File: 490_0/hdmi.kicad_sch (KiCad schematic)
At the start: 8 parts, among them J24 467650301, U10 EMI8142MUTAG, U11 EMI8142MUTAG

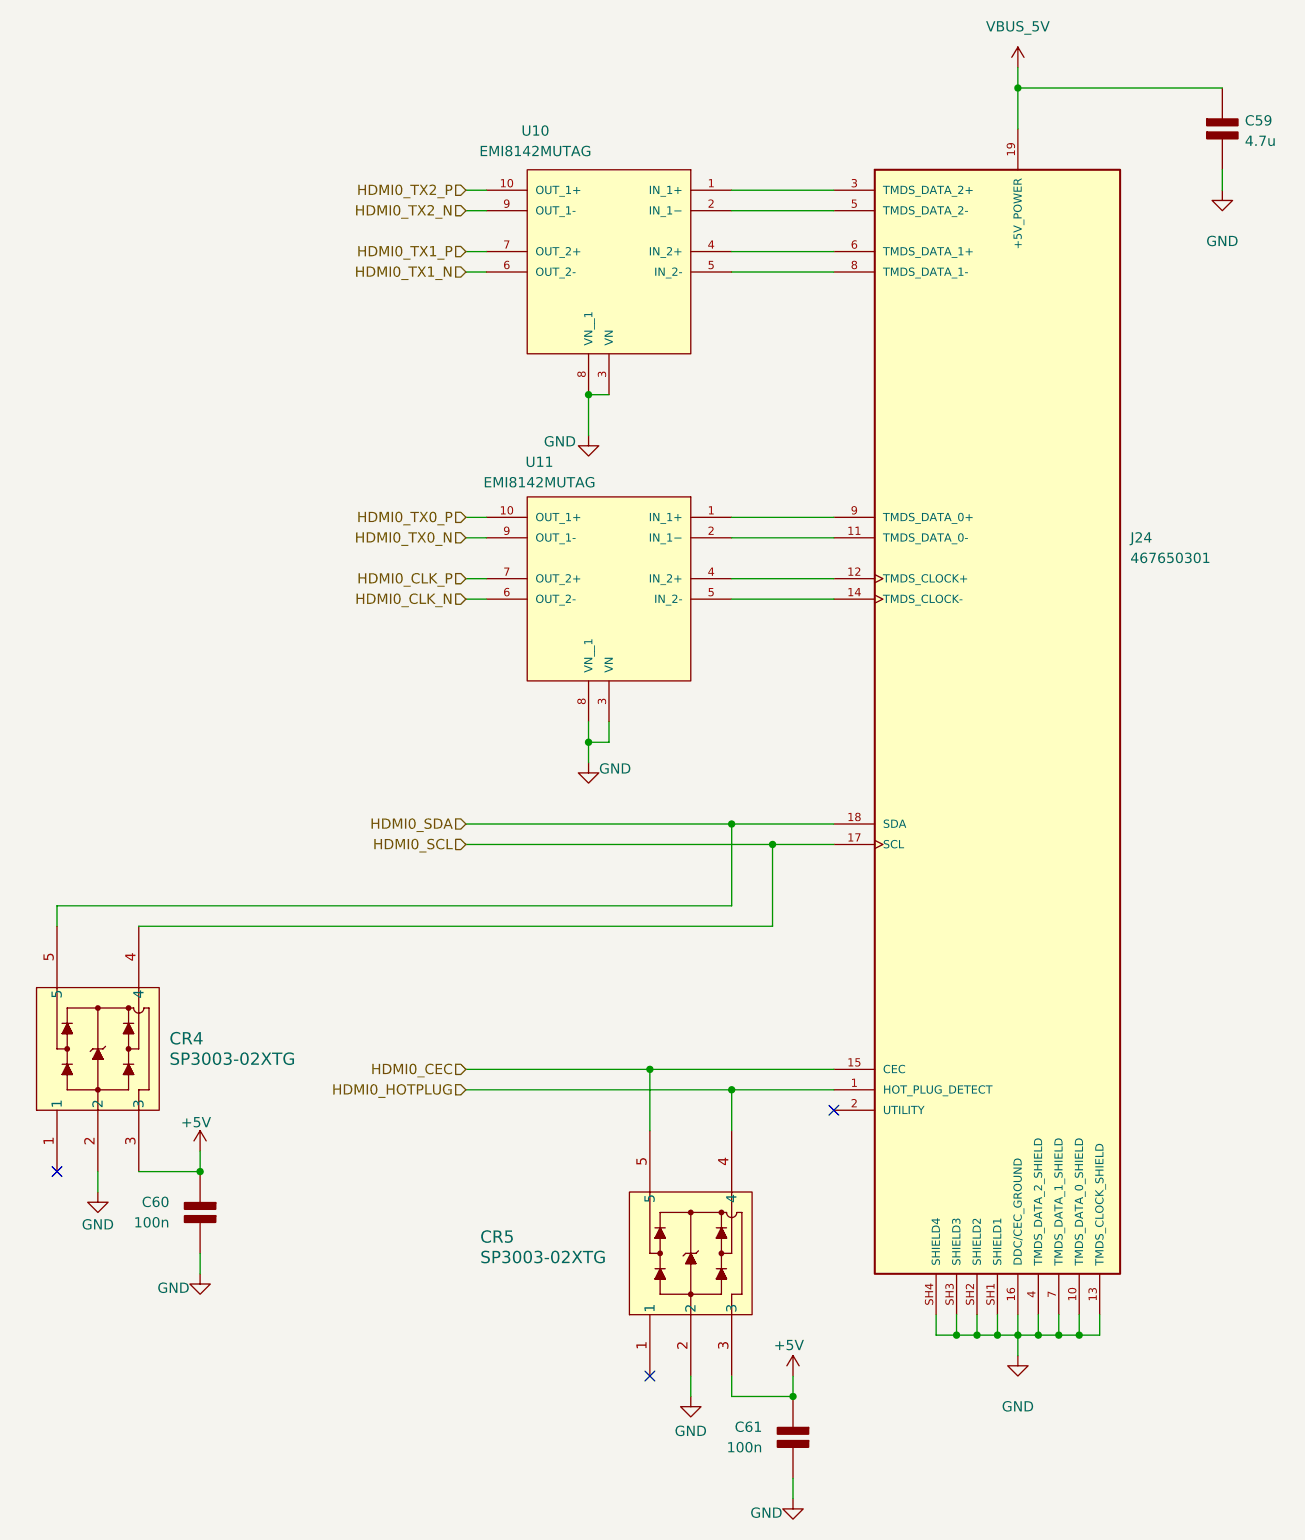
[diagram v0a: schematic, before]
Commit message: Implemented Dmitry comments
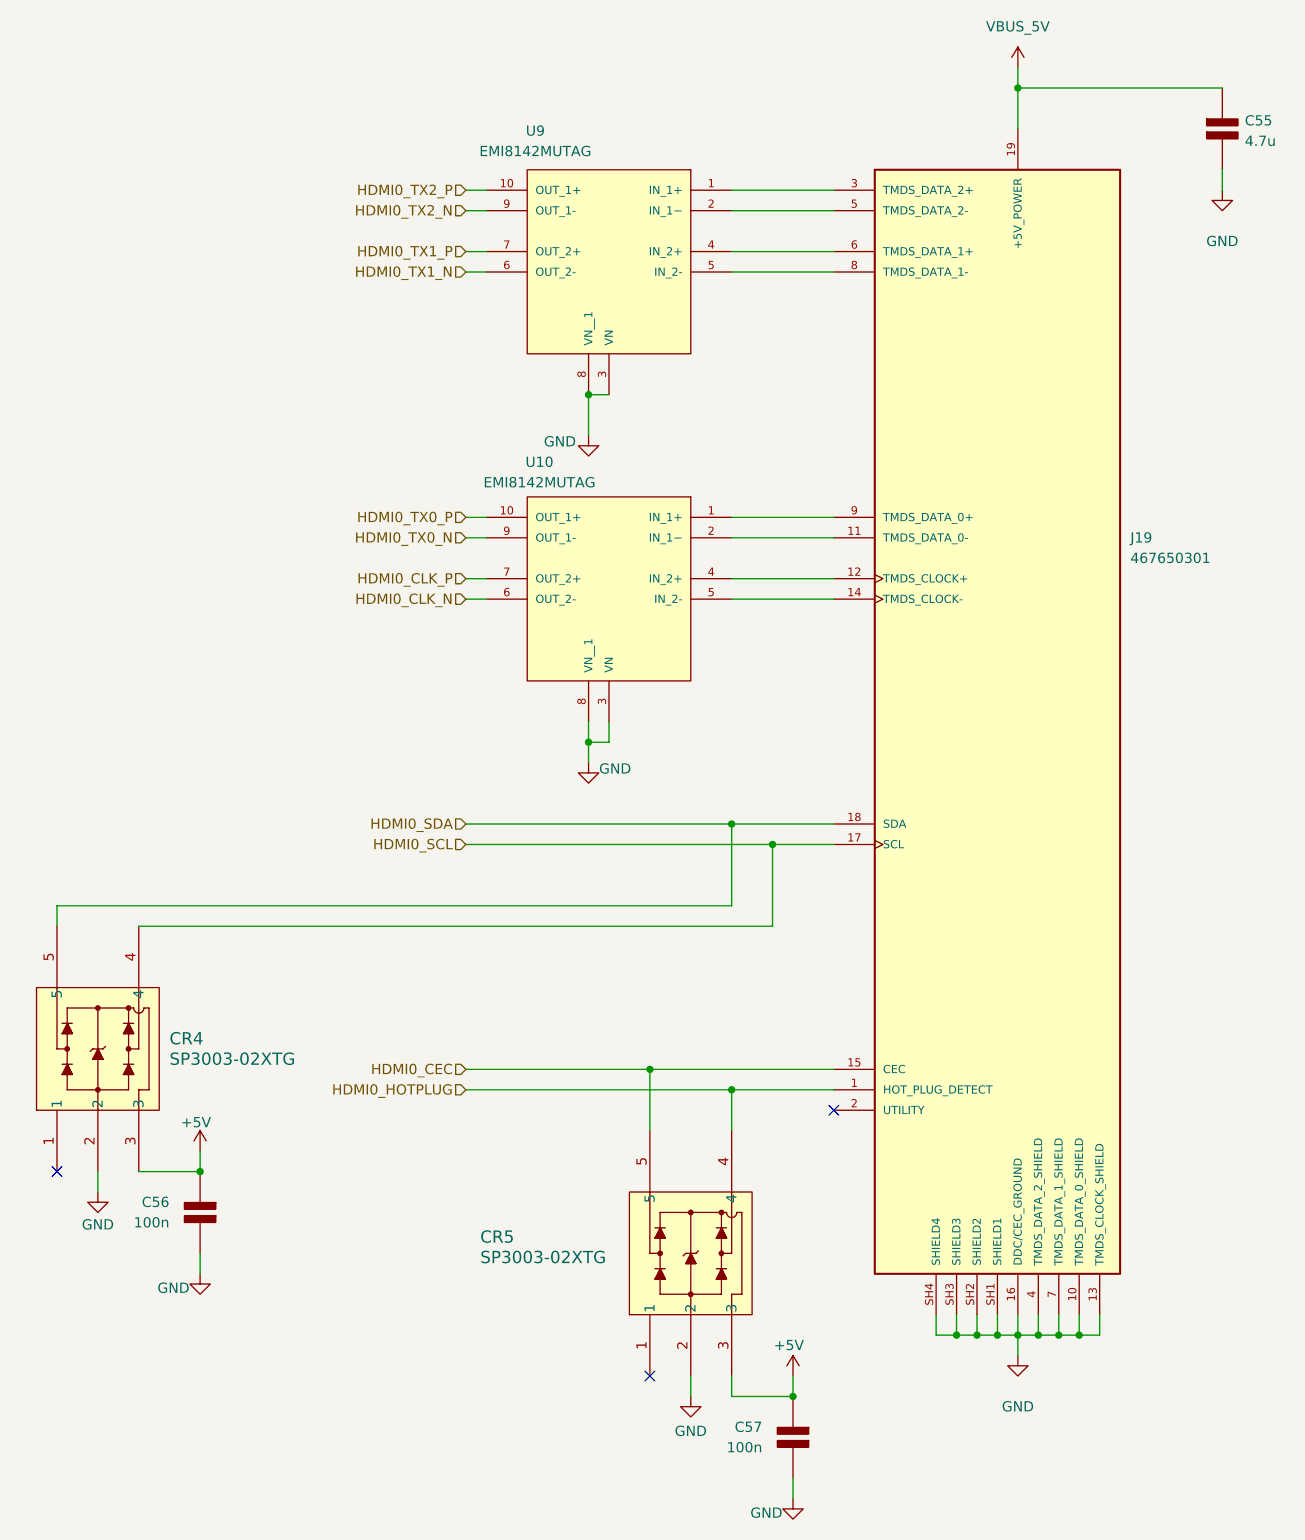
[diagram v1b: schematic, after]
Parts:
- renumbered C59 to C55, C60 to C56, C61 to C57, J24 to J19, U11 to U10, U10 to U9
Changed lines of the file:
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@@
 		(on_board yes)
 		(dnp no)
-		(property "Reference" "#PWR0154"
+		(property "Reference" "#PWR0129"
 			(at 25.4 166.37 0)
 			(effects
@@
 			(project "490_0"
 				(path "/365a82ed-827d-43e1-aa2f-b98221c4179c/f9f22bb2-829e-4ff5-89be-c4b5e2122135/a65b36cc-1b6d-4844-884d-70a990694635"
-					(reference "#PWR0154")
+					(reference "#PWR0129")
 					(unit 1)
 				)
@@
 		(dnp no)
 		(fields_autoplaced yes)
-		(property "Reference" "#PWR0149"
+		(property "Reference" "#PWR0124"
 			(at 139.7 24.13 0)
 			(effects
@@
 			(project "490_0"
 				(path "/365a82ed-827d-43e1-aa2f-b98221c4179c/f9f22bb2-829e-4ff5-89be-c4b5e2122135/a65b36cc-1b6d-4844-884d-70a990694635"
-					(reference "#PWR0149")
+					(reference "#PWR0124")
 					(unit 1)
 				)
@@
 		(on_board yes)
 		(dnp no)
-		(property "Reference" "#PWR0152"
+		(property "Reference" "#PWR0127"
 			(at 86.36 113.03 0)
 			(effects
@@
 			(project "490_0"
 				(path "/365a82ed-827d-43e1-aa2f-b98221c4179c/f9f22bb2-829e-4ff5-89be-c4b5e2122135/a65b36cc-1b6d-4844-884d-70a990694635"
-					(reference "#PWR0152")
+					(reference "#PWR0127")
 					(unit 1)
 				)
@@
 		(on_board yes)
 		(dnp no)
-		(property "Reference" "#PWR0153"
+		(property "Reference" "#PWR0128"
 			(at 38.1 158.75 0)
 			(effects
@@
 			(project "490_0"
 				(path "/365a82ed-827d-43e1-aa2f-b98221c4179c/f9f22bb2-829e-4ff5-89be-c4b5e2122135/a65b36cc-1b6d-4844-884d-70a990694635"
-					(reference "#PWR0153")
+					(reference "#PWR0128")
 					(unit 1)
 				)
@@
 		(dnp no)
 		(fields_autoplaced yes)
-		(property "Reference" "C60"
+		(property "Reference" "C56"
 			(at 34.29 161.2899 0)
 			(effects
@@
 			(project "490_0"
 				(path "/365a82ed-827d-43e1-aa2f-b98221c4179c/f9f22bb2-829e-4ff5-89be-c4b5e2122135/a65b36cc-1b6d-4844-884d-70a990694635"
-					(reference "C60")
+					(reference "C56")
 					(unit 1)
 				)
@@
 		(on_board yes)
 		(dnp no)
-		(property "Reference" "C59"
+		(property "Reference" "C55"
 			(at 167.894 26.924 0)
 			(effects
@@
 			(project "490_0"
 				(path "/365a82ed-827d-43e1-aa2f-b98221c4179c/f9f22bb2-829e-4ff5-89be-c4b5e2122135/a65b36cc-1b6d-4844-884d-70a990694635"
-					(reference "C59")
+					(reference "C55")
 					(unit 1)
 				)
@@
 		(on_board yes)
 		(dnp no)
-		(property "Reference" "#PWR0151"
+		(property "Reference" "#PWR0126"
 			(at 86.36 72.39 0)
 			(effects
@@
 			(project "490_0"
 				(path "/365a82ed-827d-43e1-aa2f-b98221c4179c/f9f22bb2-829e-4ff5-89be-c4b5e2122135/a65b36cc-1b6d-4844-884d-70a990694635"
-					(reference "#PWR0151")
+					(reference "#PWR0126")
 					(unit 1)
 				)
@@
 		(dnp no)
 		(fields_autoplaced yes)
-		(property "Reference" "C61"
+		(property "Reference" "C57"
 			(at 107.95 189.2299 0)
 			(effects
@@
 			(project "490_0"
 				(path "/365a82ed-827d-43e1-aa2f-b98221c4179c/f9f22bb2-829e-4ff5-89be-c4b5e2122135/a65b36cc-1b6d-4844-884d-70a990694635"
-					(reference "C61")
+					(reference "C57")
 					(unit 1)
 				)
@@
 		(on_board yes)
 		(dnp no)
-		(property "Reference" "#PWR0157"
+		(property "Reference" "#PWR0132"
 			(at 111.76 186.69 0)
 			(effects
@@
 			(project "490_0"
 				(path "/365a82ed-827d-43e1-aa2f-b98221c4179c/f9f22bb2-829e-4ff5-89be-c4b5e2122135/a65b36cc-1b6d-4844-884d-70a990694635"
-					(reference "#PWR0157")
+					(reference "#PWR0132")
 					(unit 1)
 				)
@@
 		(dnp no)
 		(fields_autoplaced yes)
-		(property "Reference" "J24"
+		(property "Reference" "J19"
 			(at 153.67 78.7399 0)
 			(effects
@@
 			(project ""
 				(path "/365a82ed-827d-43e1-aa2f-b98221c4179c/f9f22bb2-829e-4ff5-89be-c4b5e2122135/a65b36cc-1b6d-4844-884d-70a990694635"
-					(reference "J24")
+					(reference "J19")
 					(unit 1)
 				)
@@
 		(dnp no)
 		(fields_autoplaced yes)
-		(property "Reference" "#PWR0150"
+		(property "Reference" "#PWR0125"
 			(at 165.1 41.91 0)
 			(effects
@@
 			(project "490_0"
 				(path "/365a82ed-827d-43e1-aa2f-b98221c4179c/f9f22bb2-829e-4ff5-89be-c4b5e2122135/a65b36cc-1b6d-4844-884d-70a990694635"
-					(reference "#PWR0150")
+					(reference "#PWR0125")
 					(unit 1)
 				)
@@
 		(dnp no)
 		(fields_autoplaced yes)
-		(property "Reference" "#PWR0156"
+		(property "Reference" "#PWR0131"
 			(at 139.7 186.69 0)
 			(effects
@@
 			(project "490_0"
 				(path "/365a82ed-827d-43e1-aa2f-b98221c4179c/f9f22bb2-829e-4ff5-89be-c4b5e2122135/a65b36cc-1b6d-4844-884d-70a990694635"
-					(reference "#PWR0156")
+					(reference "#PWR0131")
 					(unit 1)
 				)
@@
 		(on_board yes)
 		(dnp no)
-		(property "Reference" "#PWR0158"
+		(property "Reference" "#PWR0133"
 			(at 99.06 191.77 0)
 			(effects
@@
 			(project "490_0"
 				(path "/365a82ed-827d-43e1-aa2f-b98221c4179c/f9f22bb2-829e-4ff5-89be-c4b5e2122135/a65b36cc-1b6d-4844-884d-70a990694635"
-					(reference "#PWR0158")
+					(reference "#PWR0133")
 					(unit 1)
 				)
@@
 		(on_board yes)
 		(dnp no)
-		(property "Reference" "U10"
+		(property "Reference" "U9"
 			(at 79.756 28.194 0)
 			(effects
@@
 			(project "490_0"
 				(path "/365a82ed-827d-43e1-aa2f-b98221c4179c/f9f22bb2-829e-4ff5-89be-c4b5e2122135/a65b36cc-1b6d-4844-884d-70a990694635"
-					(reference "U10")
+					(reference "U9")
 					(unit 1)
 				)
@@
 		(on_board yes)
 		(dnp no)
-		(property "Reference" "#PWR0155"
+		(property "Reference" "#PWR0130"
 			(at 38.1 176.53 0)
 			(effects
@@
 			(project "490_0"
 				(path "/365a82ed-827d-43e1-aa2f-b98221c4179c/f9f22bb2-829e-4ff5-89be-c4b5e2122135/a65b36cc-1b6d-4844-884d-70a990694635"
-					(reference "#PWR0155")
+					(reference "#PWR0130")
 					(unit 1)
 				)
@@
 		(on_board yes)
 		(dnp no)
-		(property "Reference" "U11"
+		(property "Reference" "U10"
 			(at 80.264 69.342 0)
 			(effects
@@
 			(project "490_0"
 				(path "/365a82ed-827d-43e1-aa2f-b98221c4179c/f9f22bb2-829e-4ff5-89be-c4b5e2122135/a65b36cc-1b6d-4844-884d-70a990694635"
-					(reference "U11")
+					(reference "U10")
 					(unit 1)
 				)
@@
 		(on_board yes)
 		(dnp no)
-		(property "Reference" "#PWR0159"
+		(property "Reference" "#PWR0134"
 			(at 111.76 204.47 0)
 			(effects
@@
 			(project "490_0"
 				(path "/365a82ed-827d-43e1-aa2f-b98221c4179c/f9f22bb2-829e-4ff5-89be-c4b5e2122135/a65b36cc-1b6d-4844-884d-70a990694635"
-					(reference "#PWR0159")
+					(reference "#PWR0134")
 					(unit 1)
 				)

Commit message: Final Fixes
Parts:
- renumbered C55 to C50, C56 to C51, C57 to C52
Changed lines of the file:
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@@
 		(on_board yes)
 		(dnp no)
-		(property "Reference" "#PWR0129"
+		(property "Reference" "#PWR0122"
 			(at 25.4 166.37 0)
 			(effects
@@
 			(project "490_0"
 				(path "/365a82ed-827d-43e1-aa2f-b98221c4179c/f9f22bb2-829e-4ff5-89be-c4b5e2122135/a65b36cc-1b6d-4844-884d-70a990694635"
-					(reference "#PWR0129")
+					(reference "#PWR0122")
 					(unit 1)
 				)
@@
 		(dnp no)
 		(fields_autoplaced yes)
-		(property "Reference" "#PWR0124"
+		(property "Reference" "#PWR0117"
 			(at 139.7 24.13 0)
 			(effects
@@
 			(project "490_0"
 				(path "/365a82ed-827d-43e1-aa2f-b98221c4179c/f9f22bb2-829e-4ff5-89be-c4b5e2122135/a65b36cc-1b6d-4844-884d-70a990694635"
-					(reference "#PWR0124")
+					(reference "#PWR0117")
 					(unit 1)
 				)
@@
 		(on_board yes)
 		(dnp no)
-		(property "Reference" "#PWR0127"
+		(property "Reference" "#PWR0120"
 			(at 86.36 113.03 0)
 			(effects
@@
 			(project "490_0"
 				(path "/365a82ed-827d-43e1-aa2f-b98221c4179c/f9f22bb2-829e-4ff5-89be-c4b5e2122135/a65b36cc-1b6d-4844-884d-70a990694635"
-					(reference "#PWR0127")
+					(reference "#PWR0120")
 					(unit 1)
 				)
@@
 		(on_board yes)
 		(dnp no)
-		(property "Reference" "#PWR0128"
+		(property "Reference" "#PWR0121"
 			(at 38.1 158.75 0)
 			(effects
@@
 			(project "490_0"
 				(path "/365a82ed-827d-43e1-aa2f-b98221c4179c/f9f22bb2-829e-4ff5-89be-c4b5e2122135/a65b36cc-1b6d-4844-884d-70a990694635"
-					(reference "#PWR0128")
+					(reference "#PWR0121")
 					(unit 1)
 				)
@@
 		(dnp no)
 		(fields_autoplaced yes)
-		(property "Reference" "C56"
+		(property "Reference" "C51"
 			(at 34.29 161.2899 0)
 			(effects
@@
 			(project "490_0"
 				(path "/365a82ed-827d-43e1-aa2f-b98221c4179c/f9f22bb2-829e-4ff5-89be-c4b5e2122135/a65b36cc-1b6d-4844-884d-70a990694635"
-					(reference "C56")
+					(reference "C51")
 					(unit 1)
 				)
@@
 		(on_board yes)
 		(dnp no)
-		(property "Reference" "C55"
+		(property "Reference" "C50"
 			(at 167.894 26.924 0)
 			(effects
@@
 			(project "490_0"
 				(path "/365a82ed-827d-43e1-aa2f-b98221c4179c/f9f22bb2-829e-4ff5-89be-c4b5e2122135/a65b36cc-1b6d-4844-884d-70a990694635"
-					(reference "C55")
+					(reference "C50")
 					(unit 1)
 				)
@@
 		(on_board yes)
 		(dnp no)
-		(property "Reference" "#PWR0126"
+		(property "Reference" "#PWR0119"
 			(at 86.36 72.39 0)
 			(effects
@@
 			(project "490_0"
 				(path "/365a82ed-827d-43e1-aa2f-b98221c4179c/f9f22bb2-829e-4ff5-89be-c4b5e2122135/a65b36cc-1b6d-4844-884d-70a990694635"
-					(reference "#PWR0126")
+					(reference "#PWR0119")
 					(unit 1)
 				)
@@
 		(dnp no)
 		(fields_autoplaced yes)
-		(property "Reference" "C57"
+		(property "Reference" "C52"
 			(at 107.95 189.2299 0)
 			(effects
@@
 			(project "490_0"
 				(path "/365a82ed-827d-43e1-aa2f-b98221c4179c/f9f22bb2-829e-4ff5-89be-c4b5e2122135/a65b36cc-1b6d-4844-884d-70a990694635"
-					(reference "C57")
+					(reference "C52")
 					(unit 1)
 				)
@@
 		(on_board yes)
 		(dnp no)
-		(property "Reference" "#PWR0132"
+		(property "Reference" "#PWR0125"
 			(at 111.76 186.69 0)
 			(effects
@@
 			(project "490_0"
 				(path "/365a82ed-827d-43e1-aa2f-b98221c4179c/f9f22bb2-829e-4ff5-89be-c4b5e2122135/a65b36cc-1b6d-4844-884d-70a990694635"
-					(reference "#PWR0132")
+					(reference "#PWR0125")
 					(unit 1)
 				)
@@
 		(dnp no)
 		(fields_autoplaced yes)
-		(property "Reference" "#PWR0125"
+		(property "Reference" "#PWR0118"
 			(at 165.1 41.91 0)
 			(effects
@@
 			(project "490_0"
 				(path "/365a82ed-827d-43e1-aa2f-b98221c4179c/f9f22bb2-829e-4ff5-89be-c4b5e2122135/a65b36cc-1b6d-4844-884d-70a990694635"
-					(reference "#PWR0125")
+					(reference "#PWR0118")
 					(unit 1)
 				)
@@
 		(dnp no)
 		(fields_autoplaced yes)
-		(property "Reference" "#PWR0131"
+		(property "Reference" "#PWR0124"
 			(at 139.7 186.69 0)
 			(effects
@@
 			(project "490_0"
 				(path "/365a82ed-827d-43e1-aa2f-b98221c4179c/f9f22bb2-829e-4ff5-89be-c4b5e2122135/a65b36cc-1b6d-4844-884d-70a990694635"
-					(reference "#PWR0131")
+					(reference "#PWR0124")
 					(unit 1)
 				)
@@
 		(on_board yes)
 		(dnp no)
-		(property "Reference" "#PWR0133"
+		(property "Reference" "#PWR0126"
 			(at 99.06 191.77 0)
 			(effects
@@
 			(project "490_0"
 				(path "/365a82ed-827d-43e1-aa2f-b98221c4179c/f9f22bb2-829e-4ff5-89be-c4b5e2122135/a65b36cc-1b6d-4844-884d-70a990694635"
-					(reference "#PWR0133")
+					(reference "#PWR0126")
 					(unit 1)
 				)
@@
 		(on_board yes)
 		(dnp no)
-		(property "Reference" "#PWR0130"
+		(property "Reference" "#PWR0123"
 			(at 38.1 176.53 0)
 			(effects
@@
 			(project "490_0"
 				(path "/365a82ed-827d-43e1-aa2f-b98221c4179c/f9f22bb2-829e-4ff5-89be-c4b5e2122135/a65b36cc-1b6d-4844-884d-70a990694635"
-					(reference "#PWR0130")
+					(reference "#PWR0123")
 					(unit 1)
 				)
@@
 		(on_board yes)
 		(dnp no)
-		(property "Reference" "#PWR0134"
+		(property "Reference" "#PWR0127"
 			(at 111.76 204.47 0)
 			(effects
@@
 			(project "490_0"
 				(path "/365a82ed-827d-43e1-aa2f-b98221c4179c/f9f22bb2-829e-4ff5-89be-c4b5e2122135/a65b36cc-1b6d-4844-884d-70a990694635"
-					(reference "#PWR0134")
+					(reference "#PWR0127")
 					(unit 1)
 				)
